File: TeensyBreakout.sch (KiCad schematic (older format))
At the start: 65 parts, among them IC1 ZLDO1117G33, IC2 NCP1117ST50T3G, J1 73725-0110BLF, J3 RJ45_LED, J4 PJ-102A, Q1 FDN340P, Q1A1 BSD223P, Q1B1 BSD223P, SW1 SW_MEC_5E, U1 Teensy4.1, U2 ESP-WROOM-02, X1 332-06, X2 Conn_01x05

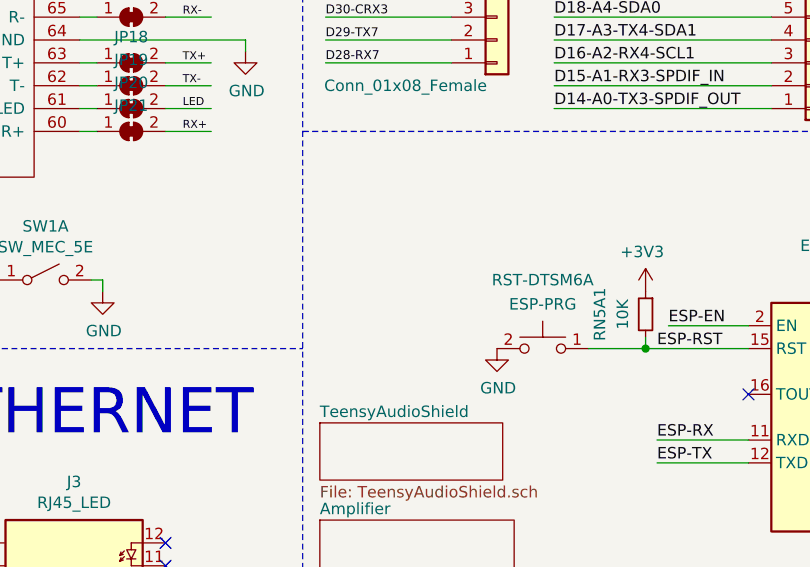
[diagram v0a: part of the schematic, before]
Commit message: removing old amp, can't buy chip
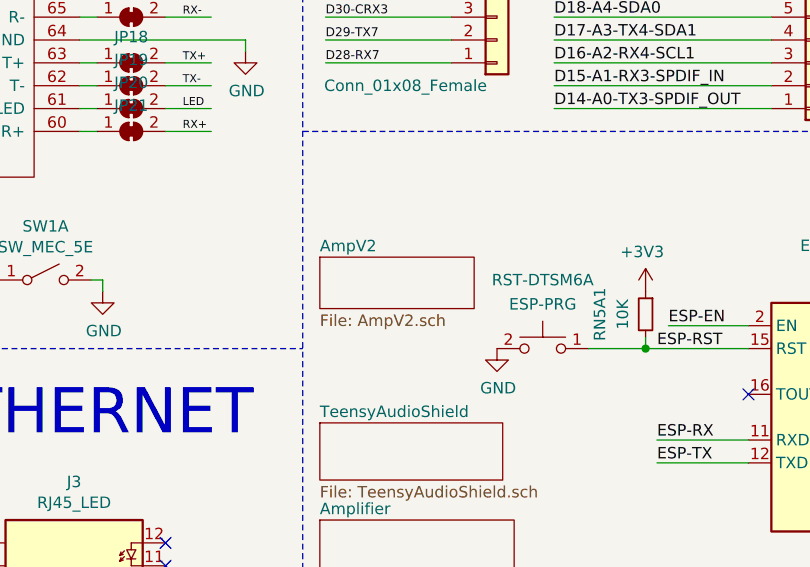
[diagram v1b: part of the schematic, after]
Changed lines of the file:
@@
 $Descr A4 11693 8268
 encoding utf-8
-Sheet 1 3
+Sheet 1 4
 Title ""
 Date ""
@@
 Wire Wire Line
 	1650 7300 1800 7300
+$Sheet
+S 7075 5000 675  225
+U 61B0849E
+F0 "AmpV2" 50
+F1 "AmpV2.sch" 50
+$EndSheet
 $EndSCHEMATC

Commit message: making layout
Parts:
- removed JP14, JP15, JP16, JP17, JP18, JP19, JP20, JP21: SolderJumper_2_Bridged, Jumper:SolderJumper-2_P1.3mm_Bridged_RoundedPad1.0x1.5mm, symbol Jumper:SolderJumper_2_Bridged
- removed X1: 332-06, Connector_PinHeader_2.54mm:PinHeader_2x03_P2.54mm_Vertical, symbol Connector_Generic:Conn_02x03_Odd_Even
- removed X2: Conn_01x05, Connector_PinHeader_2.54mm:PinHeader_1x05_P2.54mm_Vertical, symbol Connector_Generic:Conn_01x05
- added C6: 10uF, Capacitor_SMD:C_0603_1608Metric_Pad1.08x0.95mm_HandSolder, symbol Device:CP1_Small
- C1: footprint Capacitor_SMD:C_0603_1608Metric_Pad1.08x0.95mm_HandSolder -> Capacitor_THT:CP_Radial_D5.0mm_P2.50mm; symbol Device:C_Small -> Device:CP1_Small
- JP8: footprint Connector_PinSocket_2.54mm:PinSocket_2x18_P2.54mm_Vertical -> Connector_PinSocket_2.54mm:PinSocket_2x18_P2.54mm_VerticalFlipped
- L1: footprint digikey-footprints:0603 -> Resistor_SMD:R_0603_1608Metric_Pad0.98x0.95mm_HandSolder
- VIN1: footprint digikey-footprints:PinHeader_1x2_P2.54mm -> Connector_JST:JST_PH_S2B-PH-K_1x02_P2.00mm_Horizontal
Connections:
- wire segments 280 -> 274
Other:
- moved on the sheet: BT1, C3, C4, C5, IC1, IC2

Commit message: gonna try auto-route
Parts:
- removed PRG-DTSM6: ESP-PRG, Button_Switch_THT:SW_PUSH_6mm, symbol Switch:SW_Push_Dual_x2
- removed U2: ESP-WROOM-02, RF_Module:ESP-WROOM-02, symbol RF_Module:ESP-WROOM-02
- added MOD1: 2491, digikey-footprints:WIFI_Module_ESP8266_2491, symbol dk_RF-Transceiver-Modules:2491
- added PRG-DTSM1: ESP-PRG, Button_Switch_THT:SW_PUSH_6mm, symbol Switch:SW_Push_Dual_x2
- SPI1: footprint Connector_PinSocket_2.54mm:PinSocket_2x03_P2.54mm_Vertical -> CustomFootprints:PinSocket_2x03_P2.54mm_Vertical(Flipped)
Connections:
- wire segments 274 -> 287
- no-connect marks 17 -> 18
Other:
- note added: "ESP8266"
- moved on the sheet: RN5A1, RST-DTSM6A
